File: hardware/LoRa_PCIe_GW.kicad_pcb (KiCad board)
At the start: 6 copper layers, 50.9 x 30 mm, 239 parts, among them Q300 NC, Q600 NC, U100 SX1303, U201 3V3, U202 TPS62242DRV, U203 3V3, U204 STTS751, U205 NCP176BMX330TCG, U206 3V3, U300 NC, U600 ZOE-M8Q, U700 NC, U800 SX1250, U801 SAW Filter, U802 SKY66423-11, U803 SAW Filter, U805 SAW Filter, U900 SX1250, Y800 TCXO

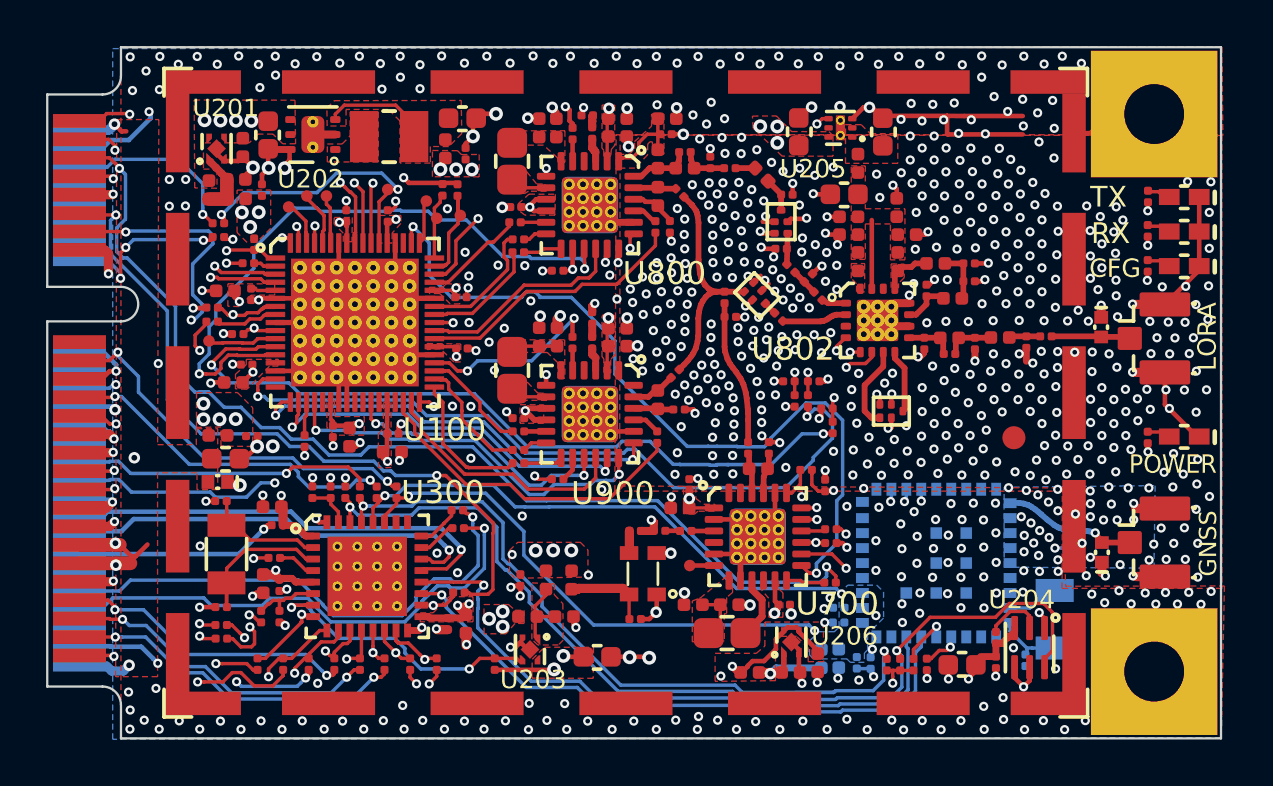
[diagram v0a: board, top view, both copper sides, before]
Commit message: Updates according to Corecell_V3 Reference design.
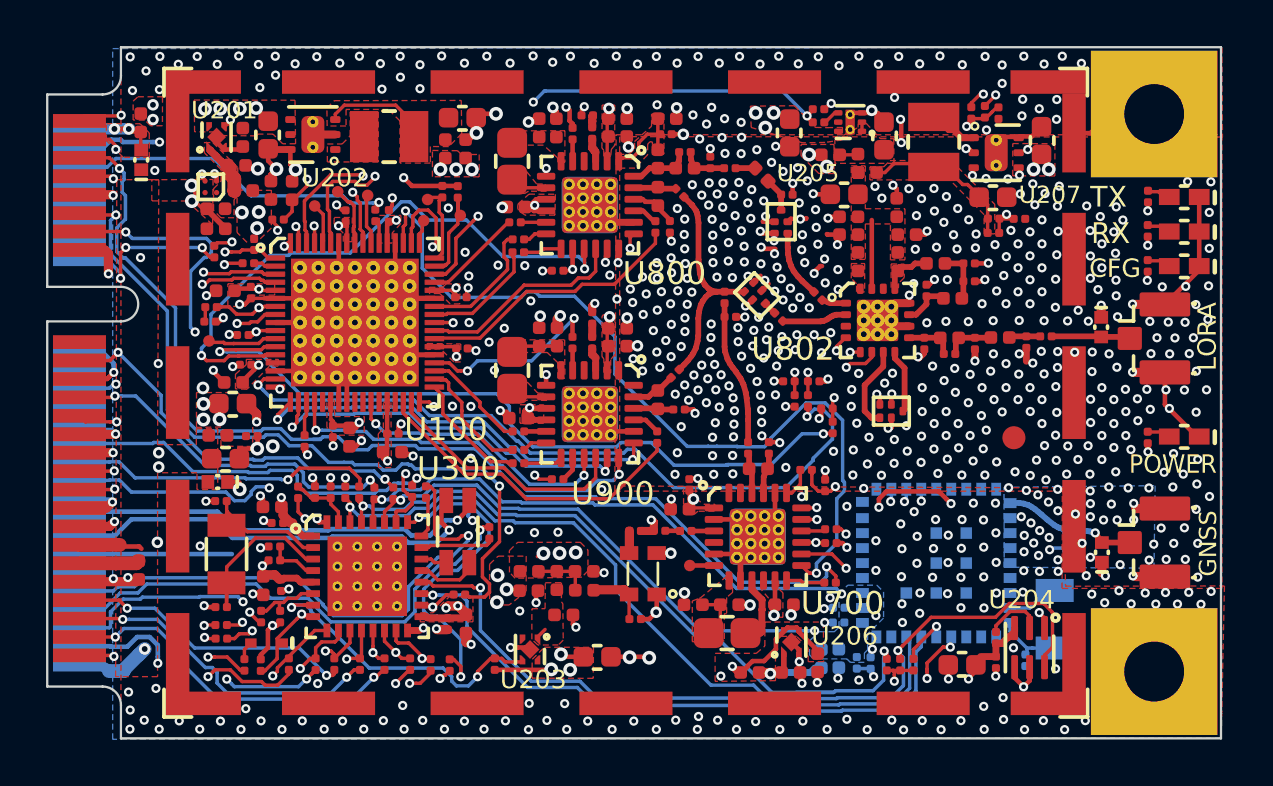
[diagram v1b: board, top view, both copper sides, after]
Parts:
- removed R802, R804: NC, LoRa_PCIe_GW:rlc_201_smd_small
- removed R803: 56pF, LoRa_PCIe_GW:ccer_201_smd_small
- removed TP2: NC, LoRa_PCIe_GW:PIN_SMD
- added C100: 100nF, LoRa_PCIe_GW:ccer_201_smd_small, F.Cu at (107.1, 111.3)
- added C200: 1uF, LoRa_PCIe_GW:ccer_402_smd_small, F.Cu at (110.6, 106.2)
- added C205: NC, LoRa_PCIe_GW:ccer_603_smd_small, F.Cu at (143.2, 104.0)
- added C209: NC, LoRa_PCIe_GW:ccer_402_smd_small, F.Cu at (107.3, 107.9)
- added C211: NC, LoRa_PCIe_GW:ccer_603_smd_small, F.Cu at (141.1, 106.5)
- added C214: NC, LoRa_PCIe_GW:ccer_201_smd_small, F.Cu at (141.1, 108.1)
- added C215: NC, LoRa_PCIe_GW:ccer_402_smd_small, F.Cu at (120.9, 123.6)
- added C305: NC, LoRa_PCIe_GW:ccer_603_smd_small, F.Cu at (108.0, 115.5)
- added C312: 100nF, LoRa_PCIe_GW:ccer_402_smd_small, F.Cu at (104.0, 122.7)
- added D101: BAT54, LoRa_PCIe_GW:SOD523, F.Cu at (109.5, 125.9)
- added D301: NC, LoRa_PCIe_GW:SLP1006P2T, F.Cu at (104.1, 104.9)
- added FB203: NC, LoRa_PCIe_GW:rlc_402_smd_small, F.Cu at (120.9, 122.8)
- added FB206: NC, LoRa_PCIe_GW:rlc_402_smd_small, F.Cu at (135.6, 105.4)
- added FB301: NC, LoRa_PCIe_GW:rlc_402_smd_small, F.Cu at (104.1, 103.3)
- added L201: NC, LoRa_PCIe_GW:LQM2HPN2R2MJ0L, F.Cu at (138.5, 104.1)
- added L300: NC, LoRa_PCIe_GW:IND_744232090, F.Cu at (117.8, 121.0)
- added R200: 0R, LoRa_PCIe_GW:rlc_201_smd_small, F.Cu at (110.0, 107.5)
- added R207: 0R, LoRa_PCIe_GW:rlc_201_smd_small, F.Cu at (133.5, 103.3)
- added R209: NC, LoRa_PCIe_GW:rlc_201_smd_small, F.Cu at (140.7, 102.8)
- added R210: NC, LoRa_PCIe_GW:rlc_201_smd_small, F.Cu at (141.3, 102.9)
- added R211: NC, LoRa_PCIe_GW:rlc_201_smd_small, F.Cu at (141.1, 107.4)
- added R212: NC, LoRa_PCIe_GW:rlc_201_smd_small, F.Cu at (142.2, 107.5)
- added R213: NC, LoRa_PCIe_GW:rlc_201_smd_small, F.Cu at (140.1, 102.8)
- added R222: NC, LoRa_PCIe_GW:rlc_402_smd_small, F.Cu at (134.0, 104.7)
- added R300: NC, LoRa_PCIe_GW:rlc_201_smd_small, F.Cu at (109.9, 122.3)
- added R325: NC, LoRa_PCIe_GW:rlc_201_smd_small, F.Cu at (110.9, 119.3)
- added R327: NC, LoRa_PCIe_GW:rlc_201_smd_small, F.Cu at (115.8, 119.3)
- added U200: NC, LoRa_PCIe_GW:DSBGA-4, F.Cu at (107.1, 106.1)
- added U207: NC, LoRa_PCIe_GW:DRV0006A_V, F.Cu at (141.2, 104.6)
- C208, C220, C221, C718, C818, C918: footprint LoRa_PCIe_GW:ccer_201_smd_small -> LoRa_PCIe_GW:ccer_402_smd_small
- C308: renamed from C300; value 10uF -> 47uF
- C309: value 100nF -> NC
- R101, R103, R107, R201, R205: value 10k -> 47k
- R108: value 0R -> 10R
- R204: footprint LoRa_PCIe_GW:rlc_402_smd_small -> LoRa_PCIe_GW:rlc_201_smd_small
- R330, R805, R807, R809: value 100R -> 1k
- moved R204 25.4 mm to (133.5, 102.7), turned to 0 degrees
- moved R332 20.7 mm to (117.5, 126.8)
- moved R101 15.7 mm to (109.3, 126.8), turned to 270 degrees
- moved R326 6.82 mm to (114.2, 107.3), turned to 270 degrees
- moved C208 2.80 mm to (123.3, 122.8), turned to 180 degrees
- moved TP5 2.56 mm to (113.9, 106.4)
- moved TP9 2.07 mm to (116.3, 107.5)
- moved R322 1.57 mm to (116.4, 119.3), turned to 270 degrees
- moved R323 1.37 mm to (119.2, 121.1), turned to 270 degrees
- moved TP1 1.13 mm to (111.6, 106.9)
- moved TP10 0.91 mm to (116.5, 106.6)
- moved R215 0.87 mm to (107.3, 107.0), turned to 180 degrees
- moved FB801 0.71 mm to (123.3, 123.6), turned to 0 degrees
- moved R301 0.66 mm to (107.2, 108.9), turned to 90 degrees
- moved C202 0.61 mm to (108.2, 105.1)
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- renumbered R202 to R215, R300 to R326, TP8 to TP10, TP9 to TP11, TP4 to TP9
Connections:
- net Net-(R304-Pad2) renamed /SCH2/MCU_BOOT0
- C718 pad 2: VDD_RADIO -> Net-(C716-Pad2)
- C809 pad 1: /SCH1/TX_RF5 -> /SCH1/TX_RF4
- C818 pad 2: VDD_RADIO -> Net-(C816-Pad2)
- C918 pad 2: VDD_RADIO -> Net-(C916-Pad2)
- PCIe_1 pad 2: VCC3V3_IN -> /SCH2/VCC5V_IN
- PCIe_1 pad 24: VCC3V3_IN -> Net-(PCIe_1-Pad24)
- R108 pad 1: PPS -> Net-(C100-Pad2)
- R108 pad 2: Net-(R108-Pad2) -> VCCIO33
- R204 pad 1: Net-(C213-Pad1) -> SX1302_CSD
- R204 pad 2: VCC_MAIN -> /SCH3/U206_EN
- R215 pad 2: VCC_MAIN -> VCC3V3_IN
- R302 pad 2: SX1302_RESET -> SX1302_RESET_HOST
- R702 pad 1: VDD_RADIO -> Net-(C716-Pad2)
- R703 pad 1: VDD_RADIO -> Net-(C716-Pad2)
- TP1 pad 1: /GPIO(0) -> Net-(TP1-Pad1)
- TP5 pad 1: /GPIO(9) -> Net-(TP5-Pad1)
- TP9 pad 1: GPIO(6) -> /GPIO(9)
- U100 pad 17: Net-(U100-Pad17) -> SX1302_PS_EN
- U100 pad 53: SX1261_DIO1 -> SX1302_GPIO_8
- U100 pad 54: Net-(U100-Pad54) -> SX1261_DIO1
- U100 pad 58: /TX_ON -> Net-(TP5-Pad1)
- U100 pad 59: /CONFIG_OK -> /RX_ON
- U100 pad 60: /RX_ON -> Net-(TP3-Pad1)
- U100 pad 63: Net-(TP3-Pad1) -> /TX_ON
- U100 pad 64: Net-(TP2-Pad1) -> Net-(TP1-Pad1)
- U100 pad 66: /GPIO(0) -> /CONFIG_OK
- U100 pad 8: Net-(R108-Pad2) -> PPS
- U201 pad 3: VCC_MAIN -> Net-(C200-Pad1)
- U205 pad 4: SX1302_CSD -> /SCH3/U205_EN
- U300 pad 21: /SCH2/USB_DN -> Net-(L300-Pad4)
- U300 pad 22: /SCH2/USB_DP -> Net-(L300-Pad1)
- U300 pad 25: Net-(U300-Pad25) -> GNSS_STANDBY
- U300 pad 26: Net-(U300-Pad26) -> SX1302_GPIO_8
- U700 pad 10: VDD_RADIO -> Net-(C716-Pad2)
- U700 pad 11: VDD_RADIO -> Net-(C716-Pad2)
- U800 pad 10: VDD_RADIO -> Net-(C816-Pad2)
- U800 pad 9: VDD_RADIO -> Net-(C816-Pad2)
- U900 pad 10: VDD_RADIO -> Net-(C916-Pad2)
- U900 pad 9: VDD_RADIO -> Net-(C916-Pad2)
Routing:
- net SX1302_PS_EN: track 0.00 -> 47.5 mm, vias 0 -> 2
- net GNSS_STANDBY: track 1.70 -> 39.0 mm, vias 1 -> 4
- net Net-(PCIe_1-Pad25): track 49.5 -> 27.2 mm
- net Net-(C716-Pad2): track 6.51 -> 25.6 mm, vias 2 -> 5
- net SX1302_GPIO_8: track 0.00 -> 17.2 mm, vias 0 -> 2
- net Net-(PCIe_1-Pad28): track 0.00 -> 17.1 mm, vias 0 -> 1
- net Net-(PCIe_1-Pad48): track 0.00 -> 14.3 mm, vias 0 -> 2
- net GPIO(6): track 12.0 -> 0.96 mm, vias 2 -> 0
- net /SCH3/U206_EN: track 0.00 -> 10.5 mm, vias 0 -> 2
- net Net-(C200-Pad1): track 0.00 -> 10.5 mm, vias 0 -> 3
- net Net-(C211-Pad1): track 0.00 -> 6.95 mm
- net Net-(C916-Pad2): track 6.91 -> 13.7 mm, vias 2 -> 3
- net Net-(PCIe_1-Pad6): track 7.85 -> 14.2 mm
- net Net-(C816-Pad2): track 7.00 -> 12.6 mm, vias 2 -> 3
- net VCCIO33: track 28.1 -> 32.7 mm, vias 16 -> 17
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- added copper zone on F.Cu, net /SCH2/VCC5V_IN
- added copper zone on F.Cu, net Net-(C202-Pad1)
- added copper zone on F.Cu, net Net-(C211-Pad1)
- added copper zone on In4.Cu, net VCC3V3_IN
- added copper zone on In2.Cu, net VCCCORE12
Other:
- board text added: "(SX1302/3)"
- board text added: "LoRa Gateway"
- board text added: "Rev: 1.1"
- board text added: "mPCIe Module"
- board text removed: "LoRa Gateway mPCIe Module (SX1302/3)"
- board text removed: "Rev: 1.0"

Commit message: Signed-off-by: mmilann <milan@nebra.com>
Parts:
- added C210: 100nF, LoRa_PCIe_GW:ccer_402_smd_small, F.Cu at (135.9, 104.2)
- added C216: 100nF, LoRa_PCIe_GW:ccer_402_smd_small, F.Cu at (120.9, 123.5)
- added C231: 22pF, LoRa_PCIe_GW:ccer_201_smd_small, F.Cu at (115.4, 102.4)
- added R231: 182K, LoRa_PCIe_GW:rlc_201_smd_small, F.Cu at (116.0, 102.4)
- added R232: 182K, LoRa_PCIe_GW:rlc_201_smd_small, F.Cu at (114.8, 102.4)
- C206: value 4.7uF -> 47uF
- C207, C212: value 10uF -> NC
- C213: value 4.7uF -> NC
- C215: value NC -> 47uF; footprint LoRa_PCIe_GW:ccer_402_smd_small -> LoRa_PCIe_GW:ccer_603_smd_small
- C222: value 2.2uF -> NC
- C223: value 100nF -> NC
- C225: value 1uF -> NC
- FB203: value NC -> Ferrite beads
- FB205: value Ferrite beads -> NC
- R201: value 47k -> 47K
- R205: value 47k -> NC
- R207: value 0R -> NC
- R221, R222: value NC -> 0R
- U202: value TPS62242DRV -> TPS62260DRV
- U203, U206: value 3V3 -> NC
- U204: value STTS751 -> NC
- U205: value NCP176BMX330TCG -> NC
- U600: value ZOE-M8Q -> EVA-M8M-0
- moved R303 20.0 mm to (122.8, 109.9), turned to 270 degrees
- moved C215 1.16 mm to (120.5, 124.7)
- moved C206 0.50 mm to (136.8, 103.8)
- moved R115 0.30 mm to (121.9, 109.7)
- moved L200 0.27 mm to (114.8, 104.2)
- moved U205 0.14 mm to (134.7, 103.3)
- moved R204 0.12 mm to (133.4, 102.7)
- moved L201 0.12 mm to (138.6, 104.1)
- moved R207 0.11 mm to (133.4, 103.3)
- moved FB206 0.06 mm to (135.5, 105.4)
- moved FB211 0.05 mm to (135.1, 105.0)
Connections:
- R221 pad 2: VCC_MAIN -> VCC3V3_IN
- U202 pad 3: Net-(C203-Pad1) -> Net-(C231-Pad1)
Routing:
- net RADIO_A_CLK_32M: track 30.0 -> 1.68 mm, vias 2 -> 1
- net /SCH2/RADIO_A_CLK_32M_MCU: track 2.90 -> 29.2 mm, vias 0 -> 2
- net VCC3V3_IN: track 15.8 -> 29.0 mm, vias 11 -> 13
- net VCC_MAIN: track 37.5 -> 44.6 mm
- net Net-(C231-Pad1): track 0.00 -> 3.70 mm
- net RADIO_A_NRESET: track 25.9 -> 27.0 mm
- net Net-(C203-Pad1): track 4.65 -> 3.53 mm
- net VCC_FEM1: track 1.20 -> 2.25 mm
- net GND: vias 716 -> 718
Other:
- board text added: "Rev: 1.2"
- board text removed: "Rev: 1.1"
